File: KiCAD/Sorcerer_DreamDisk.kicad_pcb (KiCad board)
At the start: 2 copper layers, 130.4 x 90.2 mm, 63 parts, among them J1 5V, J2 GND test-Point, J3 Extra Connector, U1 74LS02, U10 74LS123, U11 74LS123, U12 74LS00, U13 74LS367, U14 74LS06, U15 74LS07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

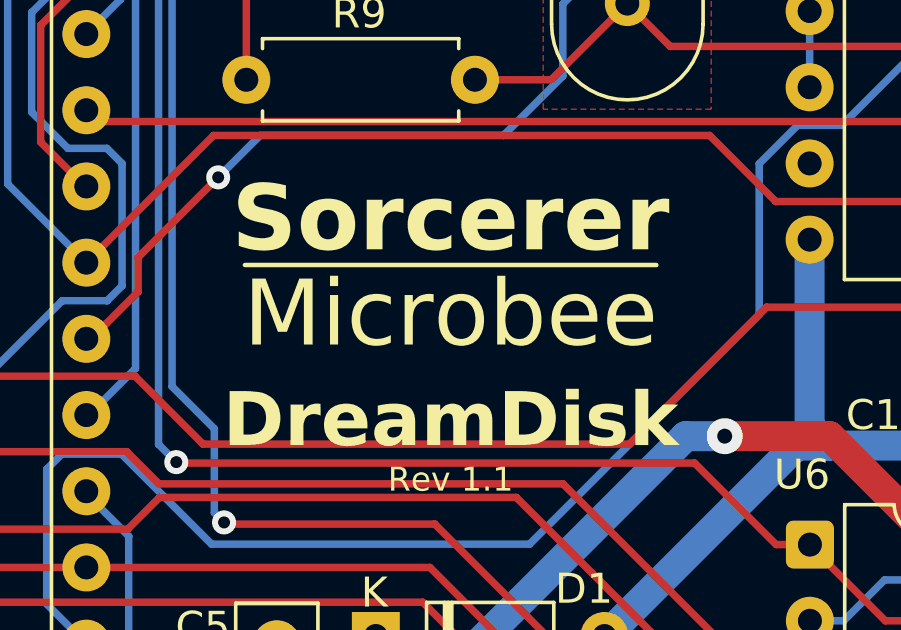
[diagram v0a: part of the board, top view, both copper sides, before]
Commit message: Update silkscreen label for MicroBee
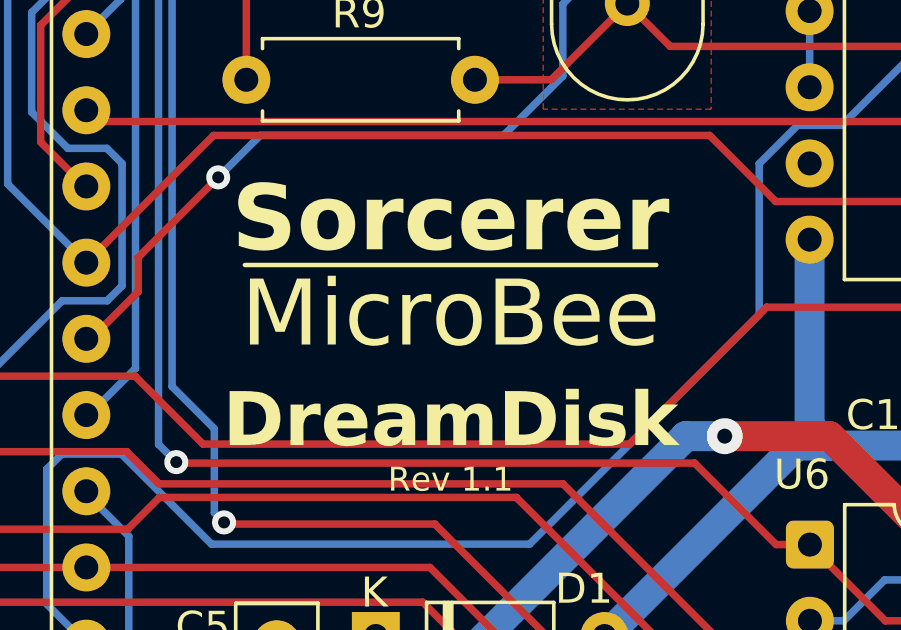
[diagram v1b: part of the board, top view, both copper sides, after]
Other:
- board text added: "MicroBee"
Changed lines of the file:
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@@
 		)
 	)
-	(gr_text "Microbee"
+	(gr_text "MicroBee"
 		(at 135.763 107.315 0)
 		(layer "F.SilkS")
